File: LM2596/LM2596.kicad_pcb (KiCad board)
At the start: 2 copper layers, 5 parts, among them U1 LM2596S-5

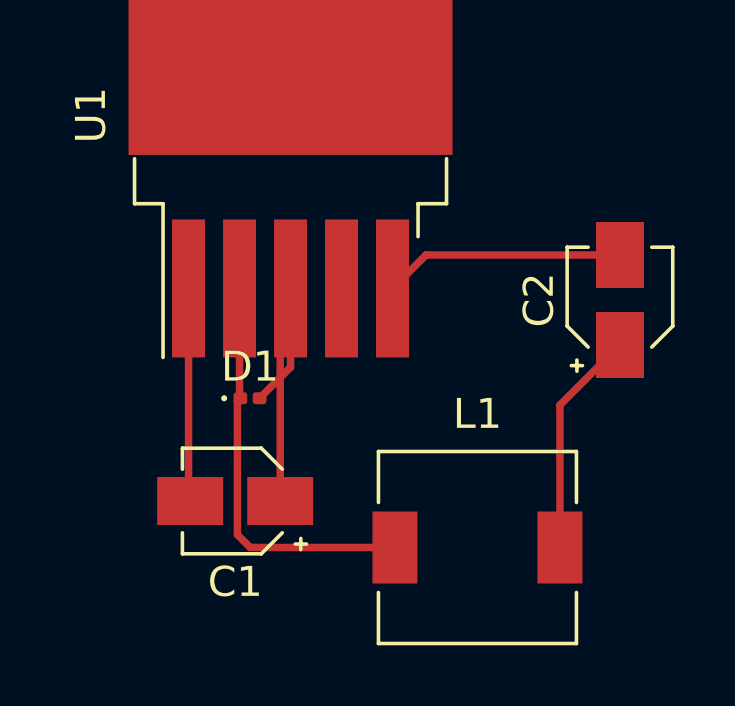
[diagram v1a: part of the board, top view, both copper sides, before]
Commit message: 15/10/2022
Ridisegnato il circuito PCB
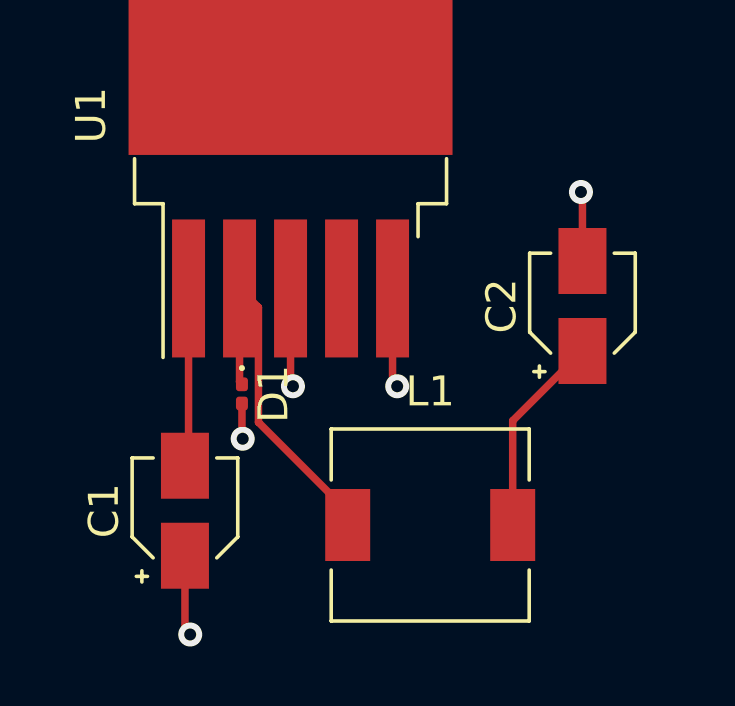
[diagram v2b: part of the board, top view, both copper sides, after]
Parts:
- moved L1 1.74 mm to (161.3, 54.3)
- moved C1 1.71 mm to (153.1, 53.8), turned to 90 degrees
- moved C2 1.27 mm to (166.4, 47.0)
- moved D1 0.30 mm to (155.0, 49.9), turned to -90 degrees
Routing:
- net GND: track 19.4 -> 13.3 mm, vias 0 -> 5
- net Net-(C1-Pad2): track 7.11 -> 5.96 mm
- net Net-(D1-Pad1): track 13.7 -> 12.6 mm
- net 5v: track 9.41 -> 8.59 mm
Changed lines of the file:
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@@
   (net 4 "Net-(D1-Pad1)")
   (footprint "Inductor_SMD:L_6.3x6.3_H3" (layer "F.Cu")
-    (at 162.875 55.05)
+    (at 161.3 54.3)
     (descr "Choke, SMD, 6.3x6.3mm 3mm height")
     (tags "Choke SMD")
@@
   )
   (footprint "Capacitor_SMD:CP_Elec_3x5.3" (layer "F.Cu")
-    (at 167.625 46.8 90)
+    (at 166.375 47 90)
     (descr "SMT capacitor, aluminium electrolytic, 3x5.3, Cornell Dubilier Electronics ")
     (tags "Capacitor Electrolytic")
@@
   )
   (footprint "Capacitor_SMD:CP_Elec_3x5.3" (layer "F.Cu")
-    (at 154.8 53.5 180)
+    (at 153.125 53.825 90)
     (descr "SMT capacitor, aluminium electrolytic, 3x5.3, Cornell Dubilier Electronics ")
     (tags "Capacitor Electrolytic")
@@
     (property "Sheetname" "")
     (attr smd)
-    (fp_text reference "C1" (at 0 -2.7) (layer "F.SilkS")
-      (effects (font (size 1 1) (thickness 0.15)))
-    )
-    (fp_text value "680uF" (at 0 2.7) (layer "F.Fab")
-      (effects (font (size 1 1) (thickness 0.15)))
-    )
-    (fp_text user "${REFERENCE}" (at 0 0) (layer "F.Fab")
+    (fp_text reference "C1" (at 0 -2.7 90) (layer "F.SilkS")
+      (effects (font (size 1 1) (thickness 0.15)))
+    )
+    (fp_text value "680uF" (at 0 2.7 90) (layer "F.Fab")
+      (effects (font (size 1 1) (thickness 0.15)))
+    )
+    (fp_text user "${REFERENCE}" (at 0 0 90) (layer "F.Fab")
       (effects (font (size 0.6 0.6) (thickness 0.09)))
     )
@@
     (fp_line (start -0.825 1.65) (end 1.65 1.65) (layer "F.Fab") (width 0.1))
     (fp_circle (center 0 0) (end 1.5 0) (layer "F.Fab") (width 0.1) (fill none))
-    (pad "1" smd rect (at -1.5 0 180) (size 2.2 1.6) (layers "F.Cu" "F.Paste" "F.Mask")
+    (pad "1" smd rect (at -1.5 0 90) (size 2.2 1.6) (layers "F.Cu" "F.Paste" "F.Mask")
       (net 1 "GND") (pintype "passive"))
-    (pad "2" smd rect (at 1.5 0 180) (size 2.2 1.6) (layers "F.Cu" "F.Paste" "F.Mask")
+    (pad "2" smd rect (at 1.5 0 90) (size 2.2 1.6) (layers "F.Cu" "F.Paste" "F.Mask")
       (net 2 "Net-(C1-Pad2)") (pintype "passive"))
     (model "${KICAD6_3DMODEL_DIR}/Capacitor_SMD.3dshapes/CP_Elec_3x5.3.wrl"
@@
   )
   (footprint "Diode_SMD:D_0201_0603Metric" (layer "F.Cu")
-    (at 155.2925 50.075)
+    (at 155.025 49.93 -90)
     (descr "Diode SMD 0201 (0603 Metric), square (rectangular) end terminal, IPC_7351 nominal, (Body size source: https://www.vishay.com/docs/20052/crcw0201e3.pdf), generated with kicad-footprint-generator")
     (tags "diode")
@@
     (property "Sheetname" "")
     (attr smd)
-    (fp_text reference "D1" (at 0 -1.05) (layer "F.SilkS")
-      (effects (font (size 1 1) (thickness 0.15)))
-    )
-    (fp_text value "D_Zener" (at 0 1.05) (layer "F.Fab")
-      (effects (font (size 1 1) (thickness 0.15)))
-    )
-    (fp_text user "${REFERENCE}" (at 0 -0.68) (layer "F.Fab")
+    (fp_text reference "D1" (at 0 -1.05 90) (layer "F.SilkS")
+      (effects (font (size 1 1) (thickness 0.15)))
+    )
+    (fp_text value "D_Zener" (at 0 1.05 90) (layer "F.Fab")
+      (effects (font (size 1 1) (thickness 0.15)))
+    )
+    (fp_text user "${REFERENCE}" (at 0 -0.68 90) (layer "F.Fab")
       (effects (font (size 0.25 0.25) (thickness 0.04)))
     )
@@
     (fp_line (start 0.3 0.15) (end -0.3 0.15) (layer "F.Fab") (width 0.1))
     (fp_line (start -0.2 0.15) (end -0.2 -0.15) (layer "F.Fab") (width 0.1))
-    (pad "" smd roundrect (at 0.345 0) (size 0.318 0.36) (layers "F.Paste") (roundrect_rratio 0.25))
-    (pad "" smd roundrect (at -0.345 0) (size 0.318 0.36) (layers "F.Paste") (roundrect_rratio 0.25))
-    (pad "1" smd roundrect (at -0.32 0) (size 0.46 0.4) (layers "F.Cu" "F.Mask") (roundrect_rratio 0.25)
+    (pad "" smd roundrect (at 0.345 0 270) (size 0.318 0.36) (layers "F.Paste") (roundrect_rratio 0.25))
+    (pad "" smd roundrect (at -0.345 0 270) (size 0.318 0.36) (layers "F.Paste") (roundrect_rratio 0.25))
+    (pad "1" smd roundrect (at -0.32 0 270) (size 0.46 0.4) (layers "F.Cu" "F.Mask") (roundrect_rratio 0.25)
       (net 4 "Net-(D1-Pad1)") (pinfunction "K") (pintype "passive"))
-    (pad "2" smd roundrect (at 0.32 0) (size 0.46 0.4) (layers "F.Cu" "F.Mask") (roundrect_rratio 0.25)
+    (pad "2" smd roundrect (at 0.32 0 270) (size 0.46 0.4) (layers "F.Cu" "F.Mask") (roundrect_rratio 0.25)
       (net 1 "GND") (pinfunction "A") (pintype "passive"))
     (model "${KICAD6_3DMODEL_DIR}/Diode_SMD.3dshapes/D_0201_0603Metric.wrl"
@@
     )
   )
-  (segment (start 156.645 49.0425) (end 156.645 46.415) (width 0.25) (layer "F.Cu") (net 1))
-  (segment (start 156.3 53.5) (end 156.3 46.76) (width 0.25) (layer "F.Cu") (net 1))
-  (segment (start 161.16 45.3) (end 160.045 46.415) (width 0.25) (layer "F.Cu") (net 1))
-  (segment (start 167.625 45.3) (end 161.16 45.3) (width 0.25) (layer "F.Cu") (net 1))
   (segment (start 156.3 46.76) (end 156.645 46.415) (width 0.25) (layer "F.Cu") (net 1))
-  (segment (start 155.6125 50.075) (end 156.645 49.0425) (width 0.25) (layer "F.Cu") (net 1))
-  (segment (start 153.245 53.445) (end 153.3 53.5) (width 0.25) (layer "F.Cu") (net 2))
-  (segment (start 153.245 46.415) (end 153.245 53.445) (width 0.25) (layer "F.Cu") (net 2))
-  (segment (start 165.625 55.05) (end 165.625 50.3) (width 0.25) (layer "F.Cu") (net 3))
-  (segment (start 165.625 50.3) (end 167.625 48.3) (width 0.25) (layer "F.Cu") (net 3))
+  (segment (start 160.045 46.415) (end 160.045 49.52) (width 0.25) (layer "F.Cu") (net 1))
+  (segment (start 155.025 50.25) (end 155.025 51.4) (width 0.25) (layer "F.Cu") (net 1))
+  (segment (start 155.025 51.4) (end 155.05 51.425) (width 0.25) (layer "F.Cu") (net 1))
+  (segment (start 156.645 49.595) (end 156.725 49.675) (width 0.25) (layer "F.Cu") (net 1))
+  (segment (start 153.125 57.775) (end 153.3 57.95) (width 0.25) (layer "F.Cu") (net 1))
+  (segment (start 156.645 46.415) (end 156.645 49.595) (width 0.25) (layer "F.Cu") (net 1))
+  (segment (start 166.375 43.25) (end 166.325 43.2) (width 0.25) (layer "F.Cu") (net 1))
+  (segment (start 160.045 49.52) (end 160.2 49.675) (width 0.25) (layer "F.Cu") (net 1))
+  (segment (start 166.375 45.5) (end 166.375 43.25) (width 0.25) (layer "F.Cu") (net 1))
+  (segment (start 153.125 55.325) (end 153.125 57.775) (width 0.25) (layer "F.Cu") (net 1))
+  (via (at 166.325 43.2) (size 0.8) (drill 0.4) (layers "F.Cu" "B.Cu") (free) (net 1))
+  (via (at 156.725 49.675) (size 0.8) (drill 0.4) (layers "F.Cu" "B.Cu") (free) (net 1))
+  (via (at 153.3 57.95) (size 0.8) (drill 0.4) (layers "F.Cu" "B.Cu") (free) (net 1))
+  (via (at 160.2 49.675) (size 0.8) (drill 0.4) (layers "F.Cu" "B.Cu") (free) (net 1))
+  (via (at 155.05 51.425) (size 0.8) (drill 0.4) (layers "F.Cu" "B.Cu") (free) (net 1))
+  (segment (start 153.245 46.415) (end 153.245 52.205) (width 0.25) (layer "F.Cu") (net 2))
+  (segment (start 153.245 52.205) (end 153.125 52.325) (width 0.25) (layer "F.Cu") (net 2))
+  (segment (start 164.05 54.3) (end 164.05 50.825) (width 0.25) (layer "F.Cu") (net 3))
+  (segment (start 164.05 50.825) (end 166.375 48.5) (width 0.25) (layer "F.Cu") (net 3))
   (segment (start 158.345 48.245) (end 158.345 46.415) (width 0.25) (layer "F.Cu") (net 3))
-  (segment (start 154.875 50.1725) (end 154.9725 50.075) (width 0.25) (layer "F.Cu") (net 4))
-  (segment (start 154.875 54.625) (end 154.875 50.1725) (width 0.25) (layer "F.Cu") (net 4))
-  (segment (start 155.3 55.05) (end 154.875 54.625) (width 0.25) (layer "F.Cu") (net 4))
-  (segment (start 160.125 55.05) (end 155.3 55.05) (width 0.25) (layer "F.Cu") (net 4))
-  (segment (start 154.945 46.415) (end 154.945 50.0475) (width 0.25) (layer "F.Cu") (net 4))
-  (segment (start 154.945 50.0475) (end 154.9725 50.075) (width 0.25) (layer "F.Cu") (net 4))
+  (segment (start 158.55 53.85) (end 155.575 50.875) (width 0.25) (layer "F.Cu") (net 4))
+  (segment (start 154.945 49.53) (end 155.025 49.61) (width 0.25) (layer "F.Cu") (net 4))
+  (segment (start 155.575 47.045) (end 154.945 46.415) (width 0.25) (layer "F.Cu") (net 4))
+  (segment (start 158.55 54.3) (end 158.55 53.85) (width 0.25) (layer "F.Cu") (net 4))
+  (segment (start 155.575 50.875) (end 155.575 47.045) (width 0.25) (layer "F.Cu") (net 4))
+  (segment (start 154.945 46.415) (end 154.945 49.53) (width 0.25) (layer "F.Cu") (net 4))
 )
